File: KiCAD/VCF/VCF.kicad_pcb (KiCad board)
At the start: 2 copper layers, 40 x 75 mm, 57 parts, among them J1 Power, J2 MJ-3502, J3 MJ-3502, J4 MJ-3502, Q1 2N3906, Q10 2N3392, Q11 2N3392, Q12 2N3392, Q2 2N3392, Q3 2N3392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

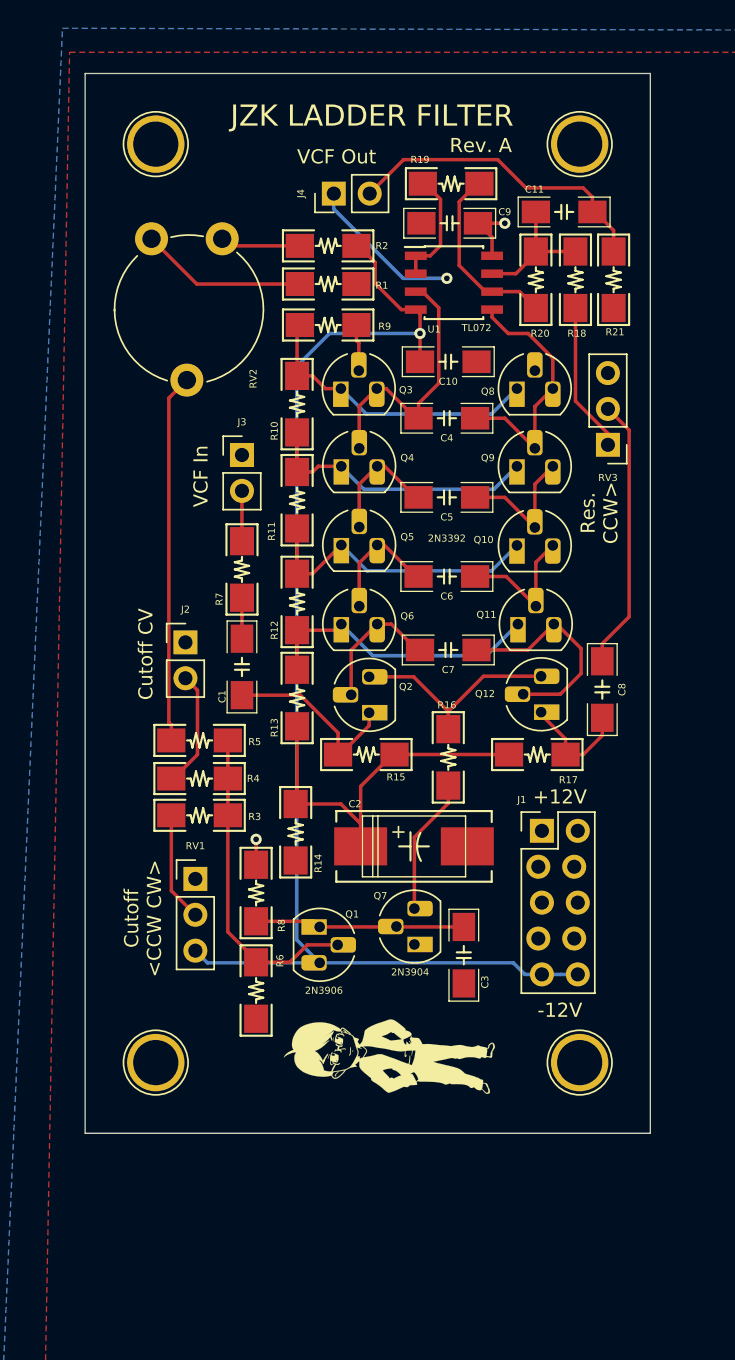
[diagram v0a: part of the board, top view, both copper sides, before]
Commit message: added voltage regulator to VCF
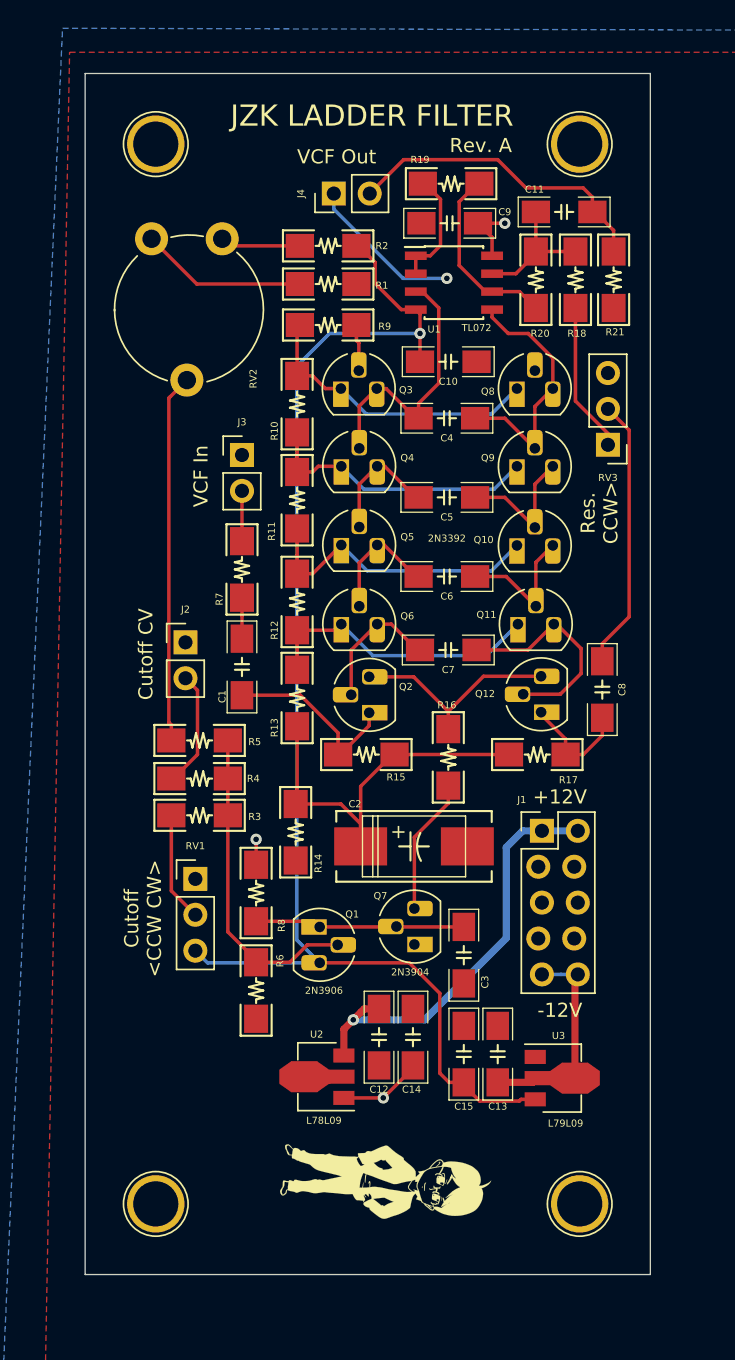
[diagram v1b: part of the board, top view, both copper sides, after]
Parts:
- added C12: 2.2uF, Synth:C_1206, F.Cu at (50.8, 98.2)
- added C13: 2.2uF, Synth:C_1206, F.Cu at (59.2, 99.4)
- added C14: 0.1uF, Synth:C_1206, F.Cu at (53.2, 98.2)
- added C15: 0.1uF, Synth:C_1206, F.Cu at (56.8, 99.4)
- added U2: L78L09, Package_TO_SOT_SMD:SOT-89-3, F.Cu at (46.8, 101.0)
- added U3: L79L09, Package_TO_SOT_SMD:SOT-89-3, F.Cu at (63.3, 101.1)
- moved REF** 10.0 mm to (65.0, 110.0)
- moved REF** 10.0 mm to (35.0, 110.0)
- moved G*** 9.40 mm to (51.4, 108.7), turned to 270 degrees
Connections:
- C10 pad 2: -12V -> -9V
- C9 pad 1: +12V -> +9V
- Q1 pad 3: -12V -> -9V
- Q3 pad 2: +12V -> +9V
- Q8 pad 2: +12V -> +9V
- R2 pad 2: -12V -> -9V
- R8 pad 1: +12V -> +9V
- R9 pad 1: +12V -> +9V
- RV1 pad 1: +12V -> +9V
- RV1 pad 3: -12V -> -9V
- U1 pad 4: -12V -> -9V
- U1 pad 8: +12V -> +9V
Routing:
- net -9V: track 0.00 -> 95.3 mm, vias 0 -> 1
- net -12V: track 91.1 -> 16.9 mm, vias 1 -> 0
- net +12V: track 9.71 -> 30.1 mm, vias 2 -> 1
- net +9V: track 0.00 -> 15.7 mm, vias 0 -> 3
- added copper zone on B.Cu, net +9V
- removed copper zone on B.Cu, net +12V
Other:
- board size 40 x 75 mm -> 40 x 85 mm

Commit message: Added RevB and VCA
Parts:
- removed G***: LOGO, Synth:ChibiLogo
- removed REF** (x4): 1pin, Connectors:1pin
- added CN1: M3_Screw, Synth:M3_Screw_Hole, F.Cu at (105.0, 110.0)
- added CN2: M3_Screw, Synth:M3_Screw_Hole, F.Cu at (155.0, 110.0)
- added CN3: M3_Screw, Synth:M3_Screw_Hole, F.Cu at (105.0, 45.0)
- added CN4: M3_Screw, Synth:M3_Screw_Hole, F.Cu at (155.0, 45.0)
- J2, J3, J4: value MJ-3502 -> 4832; footprint Connector_PinHeader_2.54mm:PinHeader_1x02_P2.54mm_Vertical -> Synth:Schurter_4832_Jack; moved to B.Cu
- RV1: value 25k -> 10k; footprint Connector_PinHeader_2.54mm:PinHeader_1x03_P2.54mm_Vertical -> Synth:Potentiometer_Bourns_PTV09A-1_Single_Vertical; moved to B.Cu
- RV3: value 25k -> 10kA; footprint Connector_PinHeader_2.54mm:PinHeader_1x03_P2.54mm_Vertical -> Synth:Potentiometer_Bourns_PTV09A-1_Single_Vertical; moved to B.Cu
- moved R3 115.8 mm to (153.7, 75.3), turned to 90 degrees
- moved RV1 115.4 mm to (150.0, 60.0), turned to 90 degrees
- moved J3 113.8 mm to (150.0, 90.0)
- moved J2 113.0 mm to (150.0, 75.0)
- moved R7 112.1 mm to (150.7, 88.6), turned to 180 degrees
- moved C1 111.4 mm to (150.7, 92.0), turned to 0 degrees
- moved R4 110.7 mm to (148.7, 75.3), turned to 90 degrees
- moved RV2 81.7 mm to (116.1, 48.2), turned to 180 degrees
- moved J4 80.9 mm to (110.0, 90.0), turned to 0 degrees
- moved R5 80.6 mm to (116.0, 98.0), turned to 90 degrees
- moved U2 77.6 mm to (124.1, 108.1)
- moved U3 77.6 mm to (140.6, 108.2)
- moved Q1 77.6 mm to (123.9, 97.5)
- moved R14 77.6 mm to (122.2, 90.8)
- moved R6 77.6 mm to (119.4, 102.0)
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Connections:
- RV1 pad 1: +9V -> -9V
- RV1 pad 3: -9V -> +9V
- RV3 pad 1: Net-(R18-Pad2) -> GND
- RV3 pad 3: GND -> Net-(R18-Pad2)
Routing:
- net VCF_Out: track 22.4 -> 88.5 mm
- net Net-(Q1-Pad2): track 22.8 -> 64.8 mm, vias 0 -> 2
- net Net-(R5-Pad2): track 26.1 -> 54.6 mm
- net Net-(C8-Pad2): track 8.13 -> 36.2 mm, vias 0 -> 1
- net Net-(R18-Pad2): track 10.6 -> 36.1 mm, vias 0 -> 1
- net Net-(C1-Pad1): track 13.4 -> 33.2 mm
- net Net-(C8-Pad1): track 19.3 -> 3.50 mm
- net -9V: track 95.3 -> 106.3 mm
- net Net-(R1-Pad1): track 11.8 -> 4.13 mm
- net GND: track 11.1 -> 18.0 mm, vias 1 -> 6
- net VCF_In: track 3.56 -> 9.34 mm
- net Net-(C7-Pad1): track 15.3 -> 10.5 mm
- net Net-(Q12-Pad3): track 15.5 -> 19.3 mm
- net +12V: track 30.1 -> 26.9 mm, vias 1 -> 0
- net Cutoff_CV: track 8.31 -> 10.9 mm
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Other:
- board size 40 x 85 mm -> 60 x 75 mm
- board text added: "Cutoff"
- board text added: "JZK LADDER FILTER Rev B"
- board text added: "Resonance"
- board text added: "VCF Input"
- board text added: "VCF Output"
- board text removed: "Cutoff <CCW CW>"
- board text removed: "JZK LADDER FILTER"
- board text removed: "Res. CCW>"
- board text removed: "Rev. A"
- board text removed: "VCF In"
- board text removed: "VCF Out"
